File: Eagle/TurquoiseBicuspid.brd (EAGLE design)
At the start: 55 x 55 mm, 14 parts, among them J0 0Ω

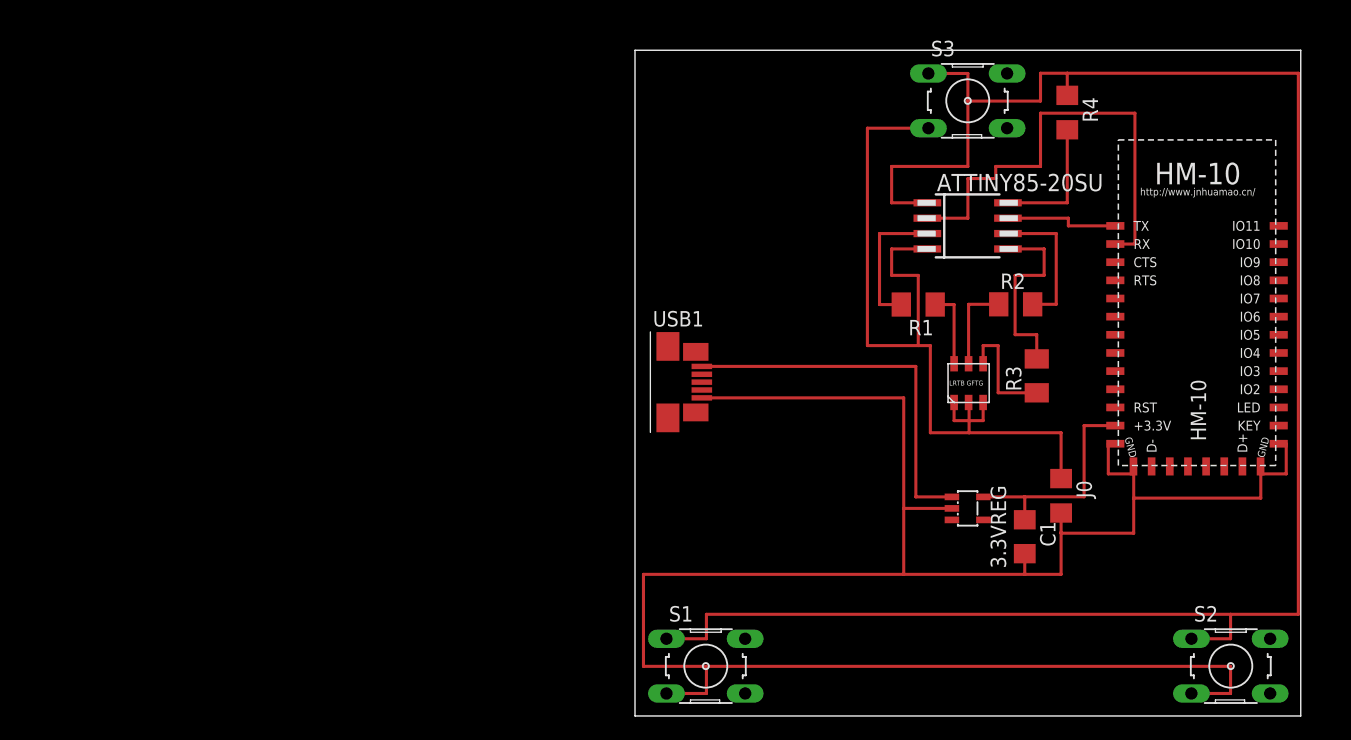
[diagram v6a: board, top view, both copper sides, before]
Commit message: fixed 5v
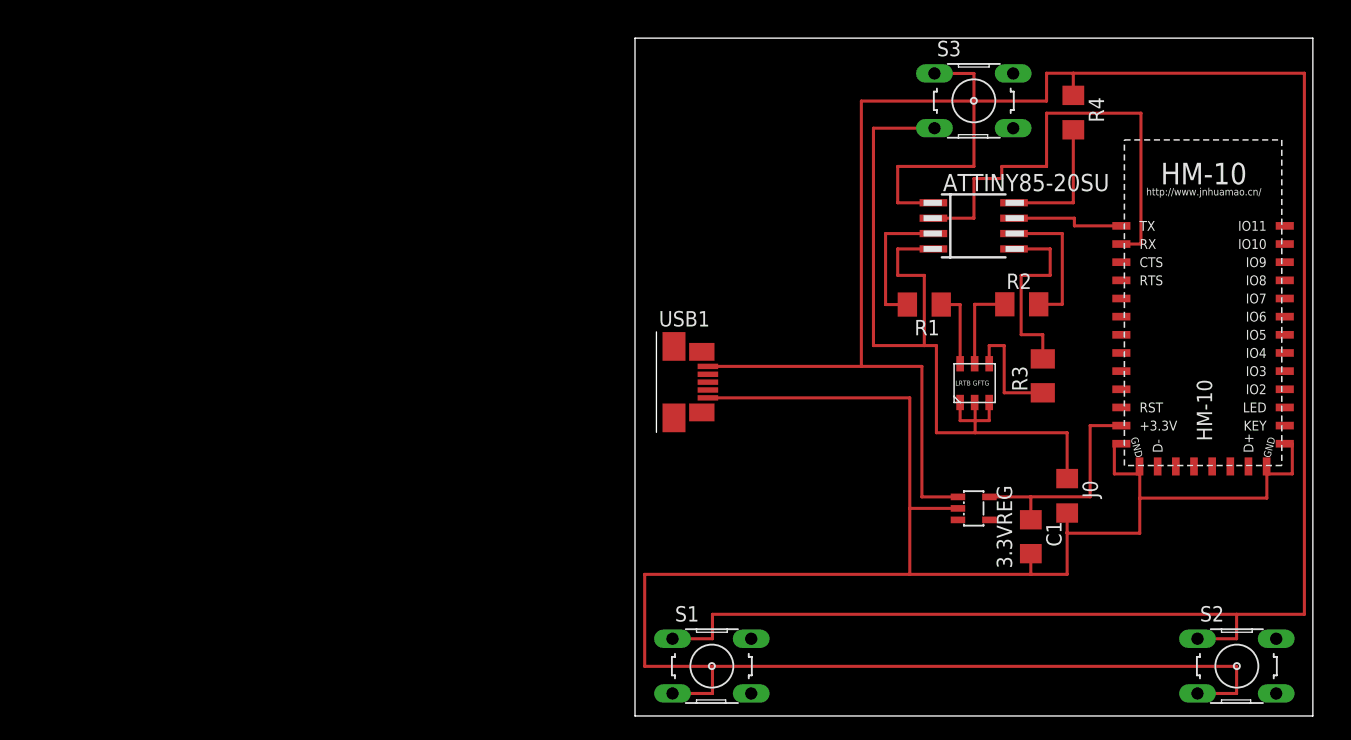
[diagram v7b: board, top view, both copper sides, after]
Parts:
- moved 3.3VREG 0.50 mm to (28.0, 17.1)
- moved ATTINY85-20SU 0.50 mm to (28.0, 40.5)
- moved C1 0.50 mm to (32.7, 14.8)
- moved HM-10 0.50 mm to (47.7, 40.5)
- moved J0 0.50 mm to (35.7, 18.2)
- moved R1 0.50 mm to (23.9, 34.0)
- moved R2 0.50 mm to (31.9, 34.0)
- moved R3 0.50 mm to (33.7, 28.1)
- moved R4 0.50 mm to (36.2, 49.9)
- moved S1 0.50 mm to (6.35, 4.12)
- moved S2 0.50 mm to (49.7, 4.12)
- moved S3 0.50 mm to (28.0, 50.8)
- moved U$1 0.50 mm to (26.4, 29.1)
- moved USB1 0.50 mm to (3.22, 27.6)
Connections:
- removed net N$14: 3.3VREG.1, USB1.1
- removed net N$4: ATTINY85-20SU.1, R4.1, S1.1, S2.1, S3.1
- net 5V: now also 3.3VREG.1, ATTINY85-20SU.1, R4.1, S1.1, S2.1, S3.1, USB1.1
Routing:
- net 5V: track 10.9 -> 232.4 mm
- net N$4: track 158.8 -> 0.00 mm
- net N$14: track 31.4 -> 0.00 mm
- net GND: track 213.1 -> 213.9 mm
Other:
- board size 55 x 55 mm -> 56 x 56 mm

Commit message: board v1.1
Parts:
- added J1, J2: 0Ω, rcl:R1206
- moved R4 14.7 mm to (21.6, 48.5)
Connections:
- net N$23 renamed BT_TX
- removed net N$1: ATTINY85-20SU.5, R3.2
- removed net N$2: ATTINY85-20SU.6, R2.2
- removed net N$3: ATTINY85-20SU.3, R1.2
- removed net N$5: ATTINY85-20SU.2, HM-10.2
- removed net N$7: R3.1, U$1.A3
- removed net N$8: R2.1, U$1.A2
- removed net N$9: R1.1, U$1.A1
- new net A1: ATTINY85-20SU.3, R1.1, R1.2, U$1.A1
- new net A2: ATTINY85-20SU.6, R2.1, R2.2, U$1.A2
- new net A3: ATTINY85-20SU.5, R3.1, R3.2, U$1.A3
- new net BT_RX: ATTINY85-20SU.2, HM-10.2, J1.1, J1.2
- new net RESET: ATTINY85-20SU.1, J2.1, J2.2, R4.2, S1.1, S2.1, S3.1
- net 5V: now also 3.3VREG.3; no longer ATTINY85-20SU.1, R4.2, S1.1, S2.1, S3.1
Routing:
- net RESET: track 0.00 -> 155.9 mm
- net 5V: track 232.4 -> 92.9 mm
- net N$5: track 38.3 -> 0.00 mm
- net BT_RX: track 0.00 -> 27.8 mm
- net A3: track 0.00 -> 26.1 mm
- net A2: track 0.00 -> 19.2 mm
- net A1: track 0.00 -> 18.1 mm
- net N$1: track 16.3 -> 0.00 mm
- net N$2: track 11.8 -> 0.00 mm
- net N$3: track 11.6 -> 0.00 mm
- net N$7: track 9.83 -> 0.00 mm
- net N$8: track 7.40 -> 0.00 mm
- net N$9: track 6.45 -> 0.00 mm
